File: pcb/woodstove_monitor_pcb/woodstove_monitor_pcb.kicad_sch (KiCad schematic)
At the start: 30 parts, among them J1 284391-2, J2 DX07S016JA1R1500, J3 284391-2, U1 ESP32-C3-WROOM-02, U2 MAX31855KASA, U3 AP63205WU, U4 AZ1117CH2-3.3

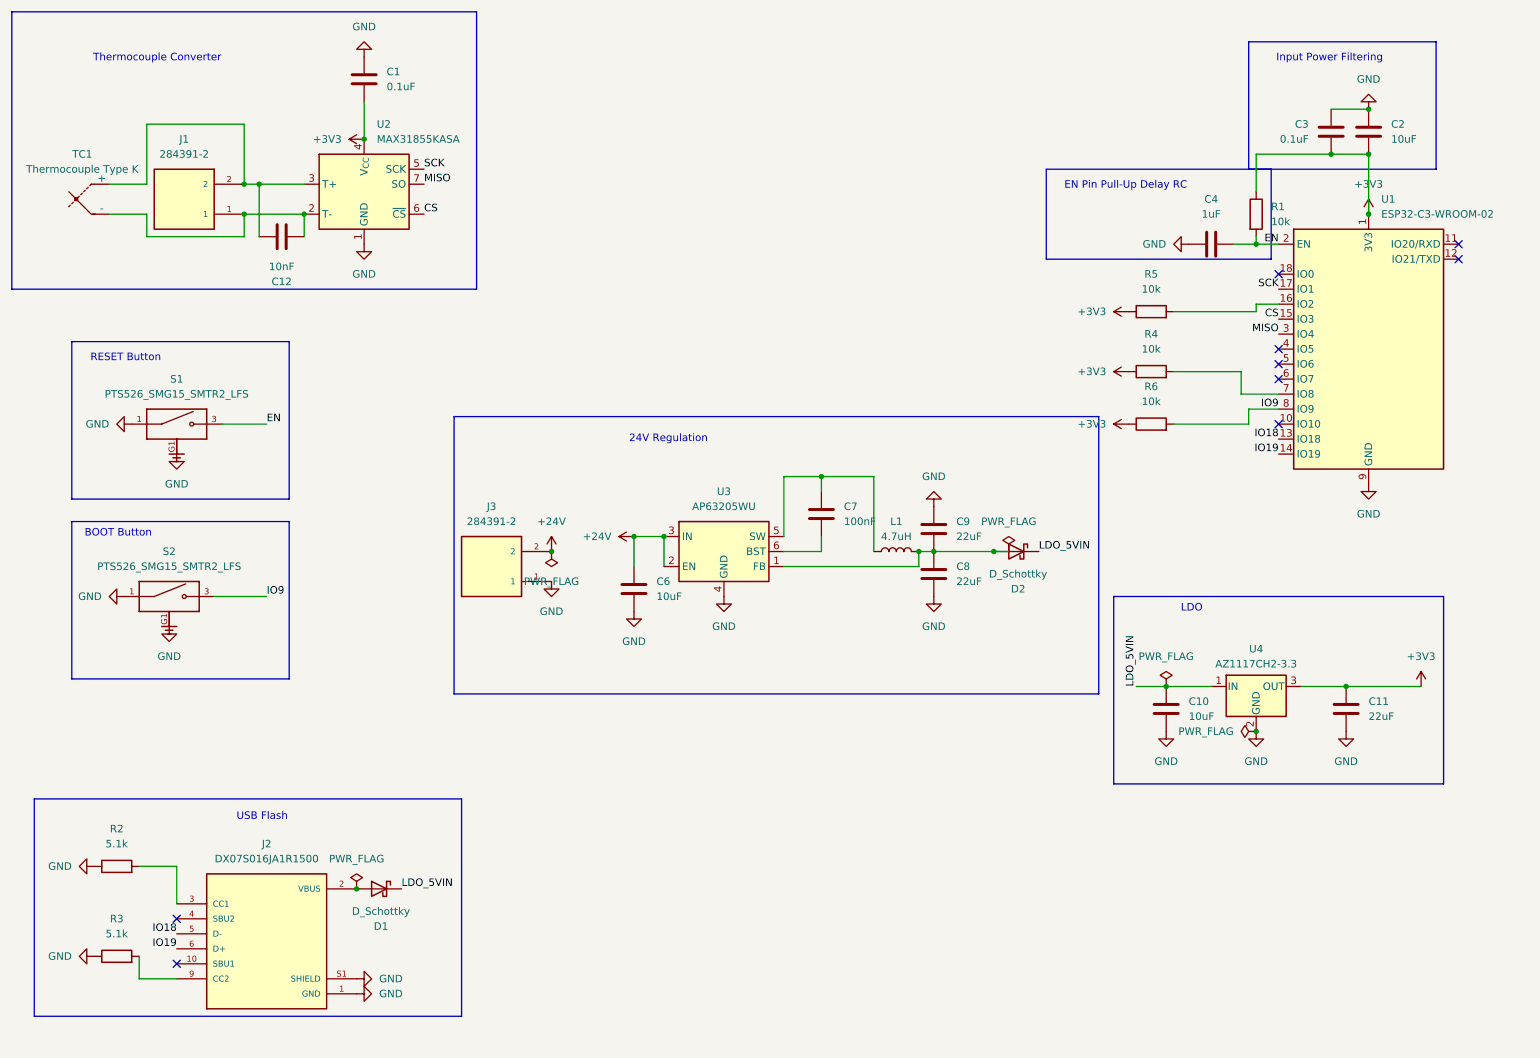
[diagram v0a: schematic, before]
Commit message: update part no. for LDO; MUST BE H2 version, not H1
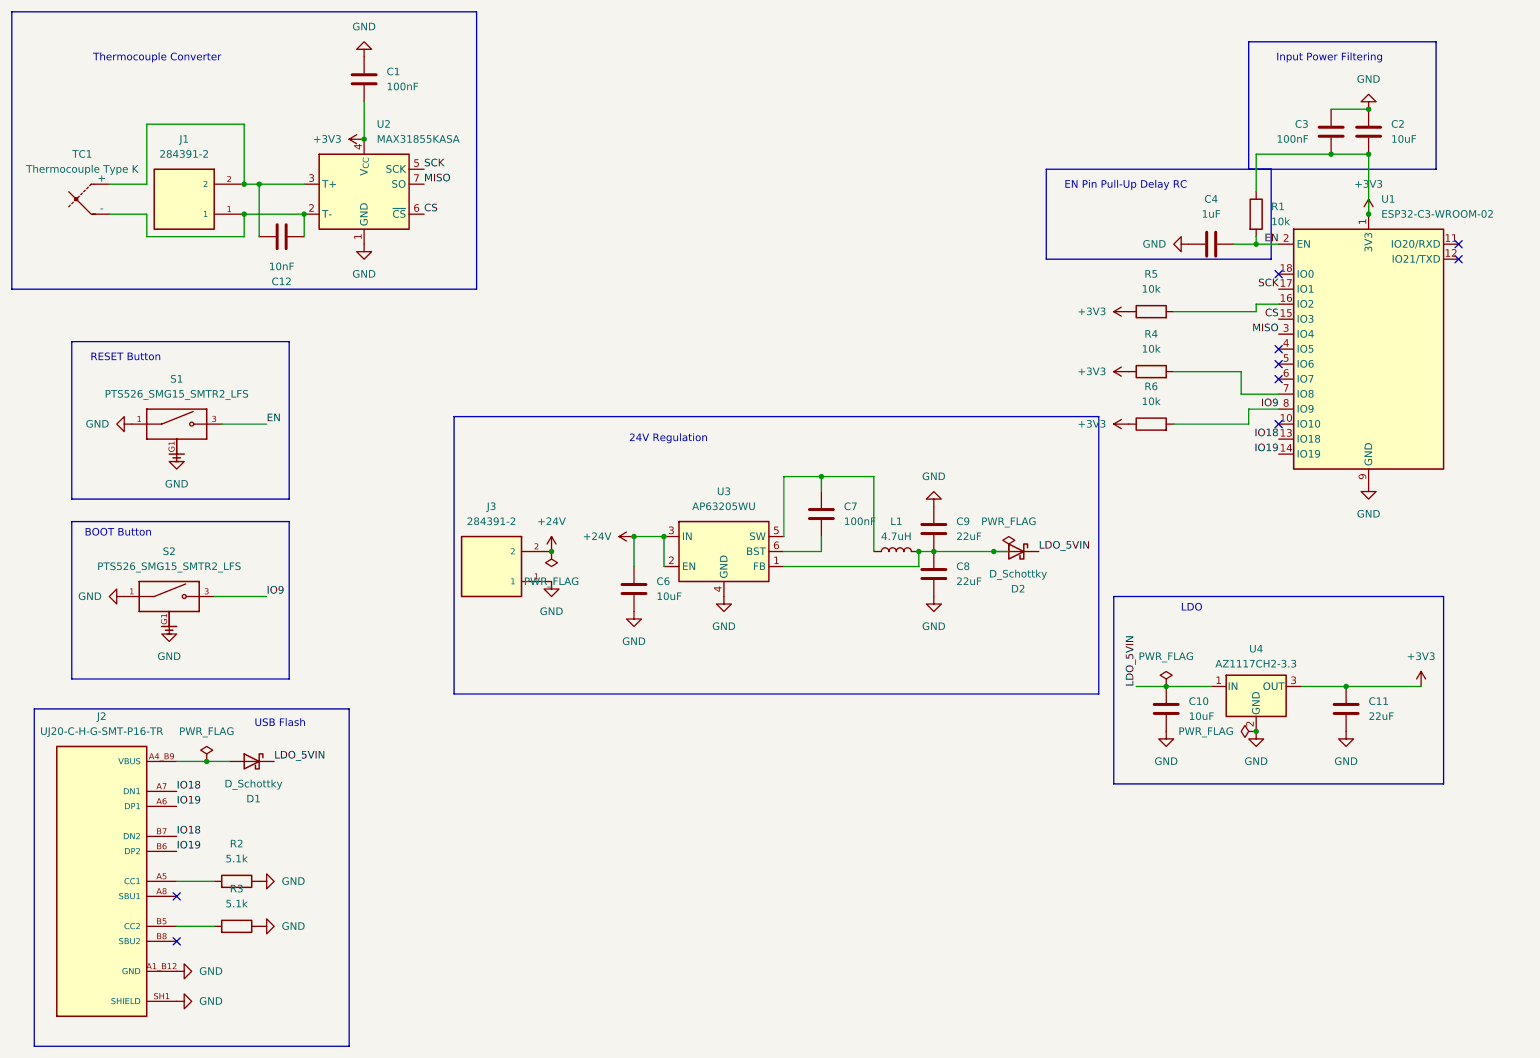
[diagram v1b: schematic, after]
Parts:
- removed J2: DX07S016JA1R1500, Connector_USB:USB_C_Receptacle_JAE_DX07S016JA1R1500, symbol USB C DX07S016JA1R1500:DX07S016JA1R1500
- added J2: UJ20-C-H-G-SMT-P16-TR, UJ20-C-H-G-SMT-P16-TR:SAMESKY_UJ20-C-H-G-SMT-P16-TR, symbol UJ20-C-H-G-SMT-P16-TR:UJ20-C-H-G-SMT-P16-TR
- C1, C3: value 0.1uF -> 100nF; Mouser Part # 80-C0805C104M5RAC -> 80-C0805C104M5RACLR
- C12: Mouser Part # 80-C0805C103J5RAC -> 80-C0805C103J5RACTM
- C4: Mouser Part # 80-C0805C105K3RAC -> 80-C0805C105K3RACTM
- C7: Mouser Part # 80-C0805C104M5RAC -> 80-C0805C104M5RACLR
- R1: Mouser Part # 303-0805WAJ0103T5E -> 303-0805S8J0103T5E
- U1: Mouser Part # (none) -> 356-ESP32C3WROOM02N4
- U4: Mouser Part # 621-AZ1117CH-3.3TRG1 -> 621-AZ1117CH2-33TRG1
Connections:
- net GND: now also J2.A12_B1 (GND), J2.A1_B12 (GND), J2.SH1 (SHIELD), J2.SH2 (SHIELD), J2.SH3 (SHIELD), J2.SH4 (SHIELD)
- net IO18: now also J2.A7 (DN1), J2.B7 (DN2)
- net IO19: now also J2.A6 (DP1), J2.B6 (DP2)
- net VBUS: now also J2.A4_B9 (VBUS), J2.A9_B4 (VBUS)
- net at R2.2: now also J2.A5 (CC1)
- net at R3.2: now also J2.B5 (CC2)
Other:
- moved on the sheet: D1, R2, R3
